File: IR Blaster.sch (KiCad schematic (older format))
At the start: 49 parts, among them CON1 AVR-ISP-6, IC1 ATMEGA328P-A, P1 FTDI Header, P2 IR Receiver, P3 Analog IN, P4 PWR, Q1 FDV303N, U1 ATSHA204A, U2 NRF24L01, U3 AT25DF512C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

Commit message: Modified design to increase LEDs from 5 @30 degrees to 7 @22.5 degrees to cover 180 degrees with greater distance using narrower angluar displacement IR LEDs.  Completed electrical traces except for optional A0-A1 inputs.
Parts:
- added D10, D11: IR LED, MySensors-BBL:LED-5MM-Horizontal, symbol LED
- added R16, R17: R, Resistors_SMD:R_0603, symbol R
- C12: footprint (none) -> Capacitors_SMD:C_0603
- D5, D6, D7, D8, D9: footprint LEDs:LED-5MM -> MySensors-BBL:LED-5MM-Horizontal
- Q1: footprint (none) -> Housings_SOT-23_SOT-143_TSOT-6:SOT-23
- U6: renamed from U?; footprint (none) -> SMD_Packages:SOT-223
- X1: footprint (none) -> Crystals_Oscillators_SMD:crystal_FA238-TSX3225
- renumbered D2 to D1, D3 to D2, D4 to D3
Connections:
- net +5V: now also R16.1, R17.1
- net GND: now also C10.2, C11.2, C12.2, C9.2, X1.3 (case)
- net at D5.1 (K), D6.1 (K), D7.1 (K)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: now also D10.1 (K), D11.1 (K)
- new net: D10.2 (A), R16.2
- new net: D11.2 (A), R17.2
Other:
- note added: "IR333-A (@IF 100mA, peak 1A), VF=1.4..1.8, RI=85mW/sr, (20 degrees)\nIR333-C (@IF 100mA, peak 1A), VF=1.4..1.8, RI=45mW/sr, (30 degrees)\nR=5V - 1.5V / 100ma = 35 ohms (15 ohms @3.3V)\nP=iV=3.5 * 0.1 = 0.35 watts (0.18 watts @3.3V)"
- note removed: "IR333-A (@IF 100mA, peak 1A), VF=1.4..1.8, RI=85mW/sr, (20 degrees)\nIR333-C (@IF 100mA, peak 1A), VF=1.4..1.8, RI=45mW/sr, (30 degrees)\nR=5V - 1.5V / 100ma = 35 ohms (15 ohms @3.3V)\nP=iV=3.5 * 0.1 = 0.35 watts (0.18 watts @5V)"
- moved on the sheet: C5, C6, D5, D6, D7, D8, D9, P1, P3, R11, R12, R13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

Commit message: Cleaned up 3D parts (power terminal block and 0603 LEDs) in preparation for v0.4 post and review.
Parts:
- P2: footprint Pin_Headers:Pin_Header_Straight_1x03 -> Socket_Strips:Socket_Strip_Straight_1x03
- P4: footprint Connect:PINHEAD1-2 -> MySensors-BBL:TerminalBlock2.54mmx2
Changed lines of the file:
@@
 F 0 "P4" H 6600 6100 50  0000 C CNN
 F 1 "PWR" V 6700 5950 50  0000 C CNN
-F 2 "Connect:PINHEAD1-2" H 6600 5950 60  0001 C CNN
+F 2 "MySensors-BBL:TerminalBlock2.54mmx2" H 6600 5950 60  0001 C CNN
 F 3 "" H 6600 5950 60  0000 C CNN
 	1    6600 5950
@@
 F 0 "P2" H 6900 1350 50  0000 C CNN
 F 1 "IR Receiver" V 7000 1150 50  0000 C CNN
-F 2 "Pin_Headers:Pin_Header_Straight_1x03" V 6700 450 60  0001 C CNN
+F 2 "Socket_Strips:Socket_Strip_Straight_1x03" V 6700 450 60  0001 C CNN
 F 3 "" H 6900 1150 60  0000 C CNN
 	1    6900 1150

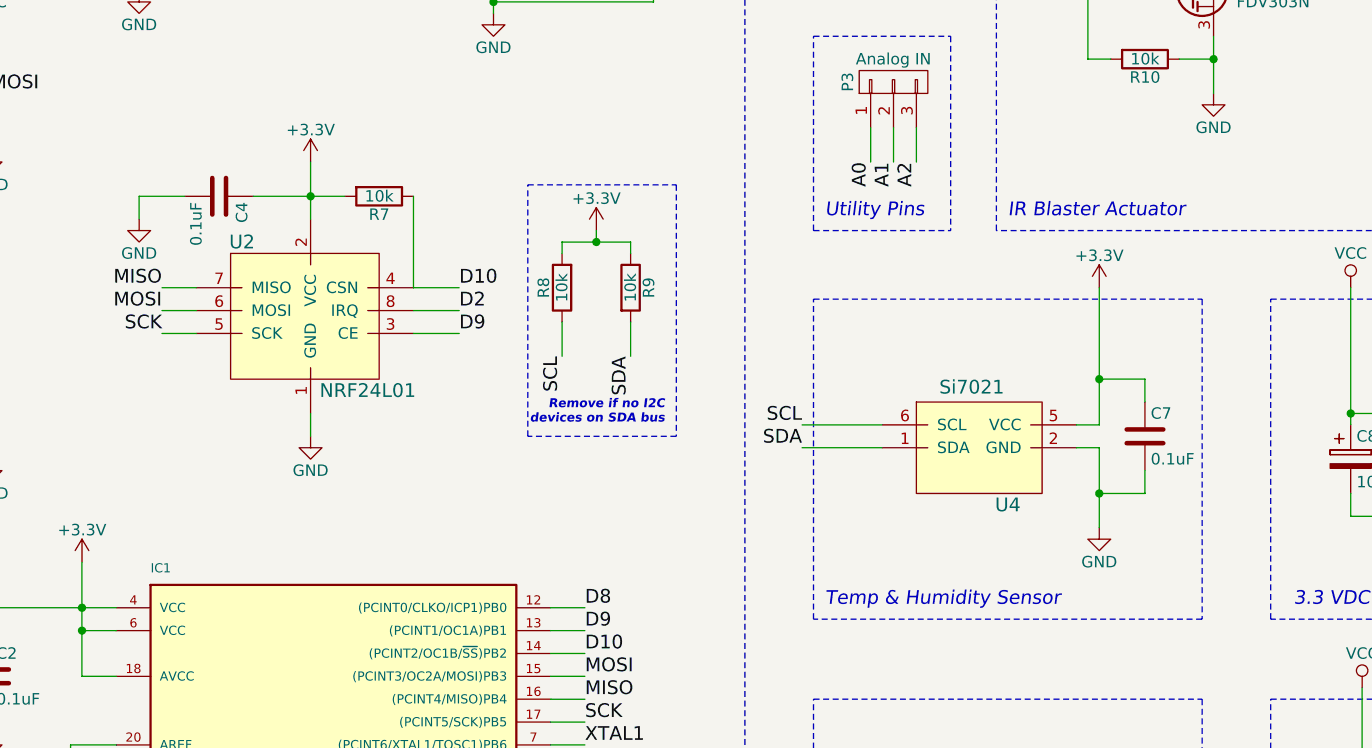
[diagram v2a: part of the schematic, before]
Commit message: Project should now be location independent users who have established mysensors part management prequisites as defined on https://github.com/mysensors-kicad/part_management.  Implemented MySensors path conventions and moved all needed parts from personal bblacey library to appropriate mysensors symbol, footprint or 3dparts github repos and modified the corresponding schematic, pcb and associated net and cmp references accordingly.
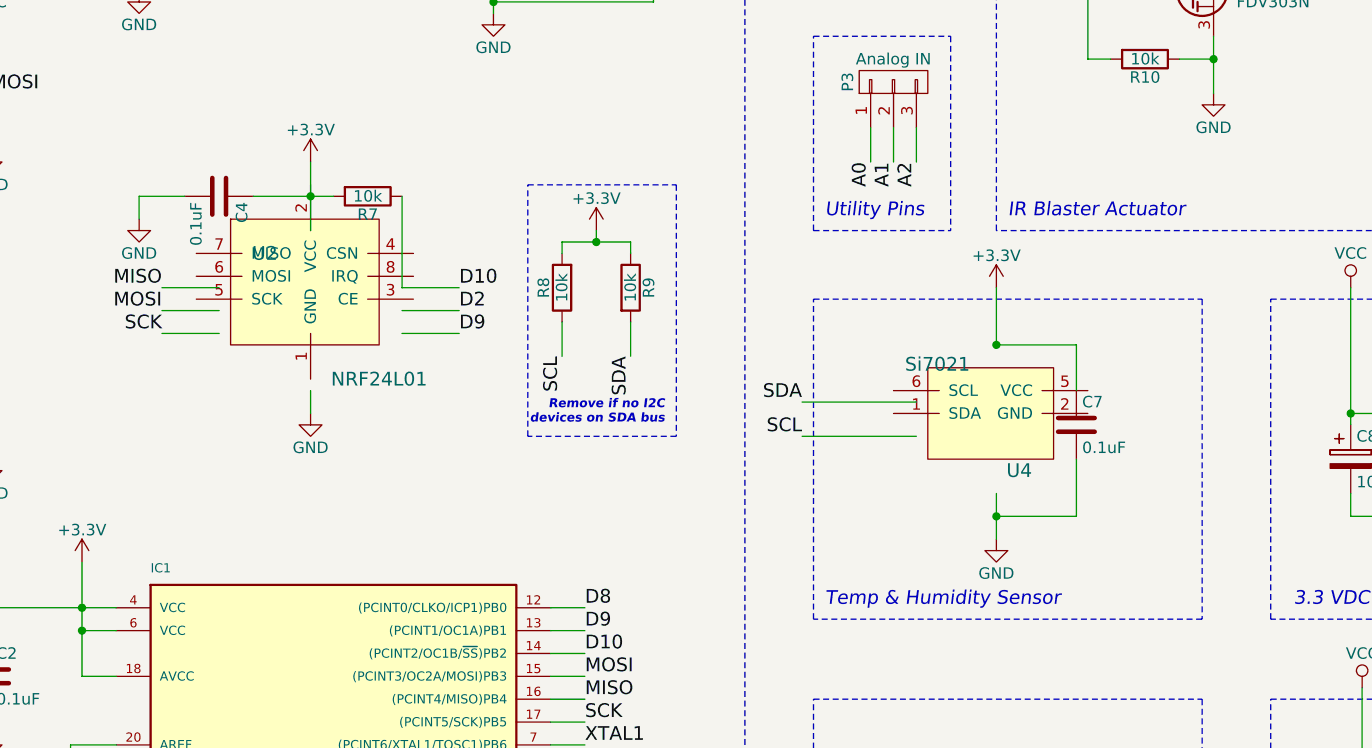
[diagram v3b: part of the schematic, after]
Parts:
- D10, D11, D5, D6, D7, D8, D9: footprint MySensors-BBL:LED-5MM-Horizontal -> mysensors_leds:LED-5MM-Horizontal
- P4: footprint MySensors-BBL:TerminalBlock2.54mmx2 -> mysensors_connectors:TerminalBlock2.54mmx2-kcswalter
- U2: footprint MySensors_Radios:NRF24L01 -> mysensors_radios:NRF24L01
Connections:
- wire segments 184 -> 182
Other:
- moved on the sheet: C7, R7, U2, U4
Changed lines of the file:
@@
 EESchema Schematic File Version 2
-LIBS:IR Blaster-rescue
 LIBS:power
 LIBS:device
@@
 LIBS:contrib
 LIBS:valves
+LIBS:mysensors_arduino
+LIBS:mysensors_logic
 LIBS:mysensors_memories
+LIBS:mysensors_network
+LIBS:mysensors_radios
+LIBS:mysensors_regulators
 LIBS:mysensors_security
-LIBS:mysensors_regulators
-LIBS:MySensors-bbl
-LIBS:MySensors
-LIBS:IR Blaster-cache
+LIBS:mysensors_sensors
 EELAYER 25 0
 EELAYER END
@@
 F 0 "D5" H 8800 1300 50  0000 C CNN
 F 1 "IR LED" H 8800 1100 50  0000 C CNN
-F 2 "MySensors-BBL:LED-5MM-Horizontal" H 8800 1200 60  0001 C CNN
+F 2 "mysensors_leds:LED-5MM-Horizontal" H 8800 1200 60  0001 C CNN
 F 3 "" H 8800 1200 60  0000 C CNN
 	1    8800 1200
@@
 F 0 "D6" H 8800 1600 50  0000 C CNN
 F 1 "IR LED" H 8800 1400 50  0000 C CNN
-F 2 "MySensors-BBL:LED-5MM-Horizontal" H 8800 1500 60  0001 C CNN
+F 2 "mysensors_leds:LED-5MM-Horizontal" H 8800 1500 60  0001 C CNN
 F 3 "" H 8800 1500 60  0000 C CNN
 	1    8800 1500
@@
 F 0 "D7" H 8800 1900 50  0000 C CNN
 F 1 "IR LED" H 8800 1700 50  0000 C CNN
-F 2 "MySensors-BBL:LED-5MM-Horizontal" H 8800 1800 60  0001 C CNN
+F 2 "mysensors_leds:LED-5MM-Horizontal" H 8800 1800 60  0001 C CNN
 F 3 "" H 8800 1800 60  0000 C CNN
 	1    8800 1800
@@
 F 0 "D8" H 8800 2200 50  0000 C CNN
 F 1 "IR LED" H 8800 2000 50  0000 C CNN
-F 2 "MySensors-BBL:LED-5MM-Horizontal" H 8800 2100 60  0001 C CNN
+F 2 "mysensors_leds:LED-5MM-Horizontal" H 8800 2100 60  0001 C CNN
 F 3 "" H 8800 2100 60  0000 C CNN
 	1    8800 2100
@@
 F 0 "D9" H 8800 2500 50  0000 C CNN
 F 1 "IR LED" H 8800 2300 50  0000 C CNN
-F 2 "MySensors-BBL:LED-5MM-Horizontal" H 8800 2400 60  0001 C CNN
+F 2 "mysensors_leds:LED-5MM-Horizontal" H 8800 2400 60  0001 C CNN
 F 3 "" H 8800 2400 60  0000 C CNN
 	1    8800 2400
@@
 L NRF24L01 U2
 U 1 1 5545493C
-P 3500 3650
-F 0 "U2" H 3200 4100 60  0000 C CNN
-F 1 "NRF24L01" H 3750 3450 60  0000 C CNN
-F 2 "MySensors_Radios:NRF24L01" H 3500 3650 60  0001 C CNN
-F 3 "" H 3500 3650 60  0000 C CNN
-	1    3500 3650
+P 3500 3500
+F 0 "U2" H 3300 3750 60  0000 C CNN
+F 1 "NRF24L01" H 3800 3200 60  0000 C CNN
+F 2 "mysensors_radios:NRF24L01" H 3500 3500 60  0001 C CNN
+F 3 "" H 3500 3500 60  0000 C CNN
+	1    3500 3500
 	1    0    0    -1
 $EndComp
@@
 F 0 "P4" H 6600 6100 50  0000 C CNN
 F 1 "PWR" V 6700 5950 50  0000 C CNN
-F 2 "MySensors-BBL:TerminalBlock2.54mmx2" H 6600 5950 60  0001 C CNN
+F 2 "mysensors_connectors:TerminalBlock2.54mmx2-kcswalter" H 6600 5950 60  0001 C CNN
 F 3 "" H 6600 5950 60  0000 C CNN
 	1    6600 5950
@@
 L GND #PWR013
 U 1 1 5548516A
-P 3500 4050
-F 0 "#PWR013" H 3500 3800 50  0001 C CNN
-F 1 "GND" H 3500 3900 50  0000 C CNN
-F 2 "" H 3500 4050 60  0000 C CNN
-F 3 "" H 3500 4050 60  0000 C CNN
-	1    3500 4050
+P 3500 3950
+F 0 "#PWR013" H 3500 3700 50  0001 C CNN
+F 1 "GND" H 3500 3800 50  0000 C CNN
+F 2 "" H 3500 3950 60  0000 C CNN
+F 3 "" H 3500 3950 60  0000 C CNN
+	1    3500 3950
 	1    0    0    -1
 $EndComp
@@
 L R R7
 U 1 1 5549A020
-P 3800 3000
-F 0 "R7" V 3880 3000 50  0000 C CNN
-F 1 "10k" V 3800 3000 50  0000 C CNN
-F 2 "Resistors_SMD:R_0603" V 3730 3000 30  0001 C CNN
-F 3 "" H 3800 3000 30  0000 C CNN
-	1    3800 3000
+P 3750 3000
+F 0 "R7" V 3830 3000 50  0000 C CNN
+F 1 "10k" V 3750 3000 50  0000 C CNN
+F 2 "Resistors_SMD:R_0603" V 3680 3000 30  0001 C CNN
+F 3 "" H 3750 3000 30  0000 C CNN
+	1    3750 3000
 	0    1    1    0
 $EndComp
@@
 Text Label 4700 6500 0    60   ~ 0
 TXD
-Text Label 5650 4100 2    60   ~ 0
+Text Label 5650 3900 2    60   ~ 0
 SDA
-Text Label 5650 4000 2    60   ~ 0
+Text Label 5650 4050 2    60   ~ 0
 SCL
 $Comp
 L +3.3V #PWR018
 U 1 1 554E1DAA
-P 6950 3400
-F 0 "#PWR018" H 6950 3250 50  0001 C CNN
-F 1 "+3.3V" H 6950 3540 50  0000 C CNN
-F 2 "" H 6950 3400 60  0000 C CNN
-F 3 "" H 6950 3400 60  0000 C CNN
-	1    6950 3400
+P 6500 3400
+F 0 "#PWR018" H 6500 3250 50  0001 C CNN
+F 1 "+3.3V" H 6500 3540 50  0000 C CNN
+F 2 "" H 6500 3400 60  0000 C CNN
+F 3 "" H 6500 3400 60  0000 C CNN
+	1    6500 3400
 	1    0    0    -1
 $EndComp
@@
 L GND #PWR019
 U 1 1 554E636C
-P 6950 4450
-F 0 "#PWR019" H 6950 4200 50  0001 C CNN
-F 1 "GND" H 6950 4300 50  0000 C CNN
-F 2 "" H 6950 4450 60  0000 C CNN
-F 3 "" H 6950 4450 60  0000 C CNN
-	1    6950 4450
+P 6500 4500
+F 0 "#PWR019" H 6500 4250 50  0001 C CNN
+F 1 "GND" H 6500 4350 50  0000 C CNN
+F 2 "" H 6500 4500 60  0000 C CNN
+F 3 "" H 6500 4500 60  0000 C CNN
+	1    6500 4500
 	1    0    0    -1
 $EndComp
@@
 L C C7
 U 1 1 554FB3A0
-P 7150 4050
-F 0 "C7" H 7175 4150 50  0000 L CNN
-F 1 "0.1uF" H 7175 3950 50  0000 L CNN
-F 2 "Capacitors_SMD:C_0603" H 7188 3900 30  0001 C CNN
-F 3 "" H 7150 4050 60  0000 C CNN
-	1    7150 4050
+P 6850 4000
+F 0 "C7" H 6875 4100 50  0000 L CNN
+F 1 "0.1uF" H 6875 3900 50  0000 L CNN
+F 2 "Capacitors_SMD:C_0603" H 6888 3850 30  0001 C CNN
+F 3 "" H 6850 4000 60  0000 C CNN
+	1    6850 4000
 	1    0    0    -1
 $EndComp
@@
 L Si7021 U4
 U 1 1 554FC23B
-P 6400 4100
-F 0 "U4" H 6550 3850 60  0000 C CNN
-F 1 "Si7021" H 6250 4400 60  0000 L TNN
-F 2 "Housings_DFN_QFN:DFN-6-1EP_3x3mm_Pitch0.95mm" H 6400 4000 60  0001 C CNN
-F 3 "" H 6400 4000 60  0000 C CNN
-	1    6400 4100
+P 6450 3950
+F 0 "U4" H 6600 3700 60  0000 C CNN
+F 1 "Si7021" H 6100 4200 60  0000 L TNN
+F 2 "Housings_DFN_QFN:DFN-6-1EP_3x3mm_Pitch0.95mm" H 6450 3850 60  0001 C CNN
+F 3 "" H 6450 3850 60  0000 C CNN
+	1    6450 3950
 	1    0    0    -1
 $EndComp
@@
 F 0 "D10" H 8800 2800 50  0000 C CNN
 F 1 "IR LED" H 8800 2600 50  0000 C CNN
-F 2 "MySensors-BBL:LED-5MM-Horizontal" H 8800 2700 60  0001 C CNN
+F 2 "mysensors_leds:LED-5MM-Horizontal" H 8800 2700 60  0001 C CNN
 F 3 "" H 8800 2700 60  0000 C CNN
 	1    8800 2700
@@
 F 0 "D11" H 8800 3100 50  0000 C CNN
 F 1 "IR LED" H 8800 2900 50  0000 C CNN
-F 2 "MySensors-BBL:LED-5MM-Horizontal" H 8800 3000 60  0001 C CNN
+F 2 "mysensors_leds:LED-5MM-Horizontal" H 8800 3000 60  0001 C CNN
 F 3 "" H 8800 3000 60  0000 C CNN
 	1    8800 3000
@@
 	4550 5000 4700 5000
 Wire Wire Line
-	3000 3500 2850 3500
-Wire Wire Line
-	3000 3400 2850 3400
-Wire Wire Line
-	3000 3600 2850 3600
-Wire Wire Line
-	3500 2850 3500 3100
-Wire Wire Line
-	3950 3400 4150 3400
-Wire Wire Line
-	3950 3500 4150 3500
-Wire Wire Line
-	3950 3600 4150 3600
-Wire Wire Line
-	3250 3000 3650 3000
+	3100 3500 2850 3500
+Wire Wire Line
+	3100 3400 2850 3400
+Wire Wire Line
+	3100 3600 2850 3600
+Wire Wire Line
+	3500 2850 3500 3150
+Wire Wire Line
+	3900 3500 4150 3500
+Wire Wire Line
+	3900 3600 4150 3600
+Wire Wire Line
+	3250 3000 3600 3000
 Connection ~ 3500 3000
 Wire Wire Line
@@
 	1700 1350 1700 1600
 Wire Wire Line
-	3950 3400 3950 3000
+	3900 3400 3900 3000
 Wire Notes Line
 	5700 3450 7400 3450
@@
 	4550 6500 4700 6500
 Wire Wire Line
-	5650 4100 6000 4100
-Wire Wire Line
-	5650 4000 6000 4000
-Wire Wire Line
-	6950 3400 6950 4000
+	5650 4050 6150 4050
+Wire Wire Line
+	5650 3900 6150 3900
+Wire Wire Line
+	6500 3400 6500 3650
 Wire Wire Line
 	4550 6050 4700 6050
@@
 	4550 6150 4700 6150
 Wire Wire Line
-	3500 4050 3500 3950
-Wire Wire Line
-	6850 4100 6950 4100
-Wire Wire Line
-	6950 4100 6950 4450
-Wire Wire Line
-	6950 4000 6850 4000
+	3500 3950 3500 3850
+Wire Wire Line
+	6500 4300 6500 4500
 Wire Wire Line
 	4550 7100 4700 7100
@@
 	1550 4000 1700 4000
 Wire Wire Line
-	7150 3900 7150 3800
-Wire Wire Line
-	7150 3800 6950 3800
-Connection ~ 6950 3800
-Wire Wire Line
-	7150 4200 7150 4300
-Wire Wire Line
-	7150 4300 6950 4300
-Connection ~ 6950 4300
+	6850 3850 6850 3650
+Wire Wire Line
+	6850 3650 6500 3650
+Connection ~ 6500 3650
+Wire Wire Line
+	6850 4150 6850 4400
+Wire Wire Line
+	6850 4400 6500 4400
+Connection ~ 6500 4400
 Wire Wire Line
 	2350 1150 3100 1150
@@
 Wire Wire Line
 	1250 5100 1250 5150
+Wire Wire Line
+	3900 3400 4150 3400
 $EndSCHEMATC
